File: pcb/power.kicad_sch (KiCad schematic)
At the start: 13 parts, among them J4 Conn_01x02, J5 ARM, U10 TPS2116DRL, U9 LM3671MF

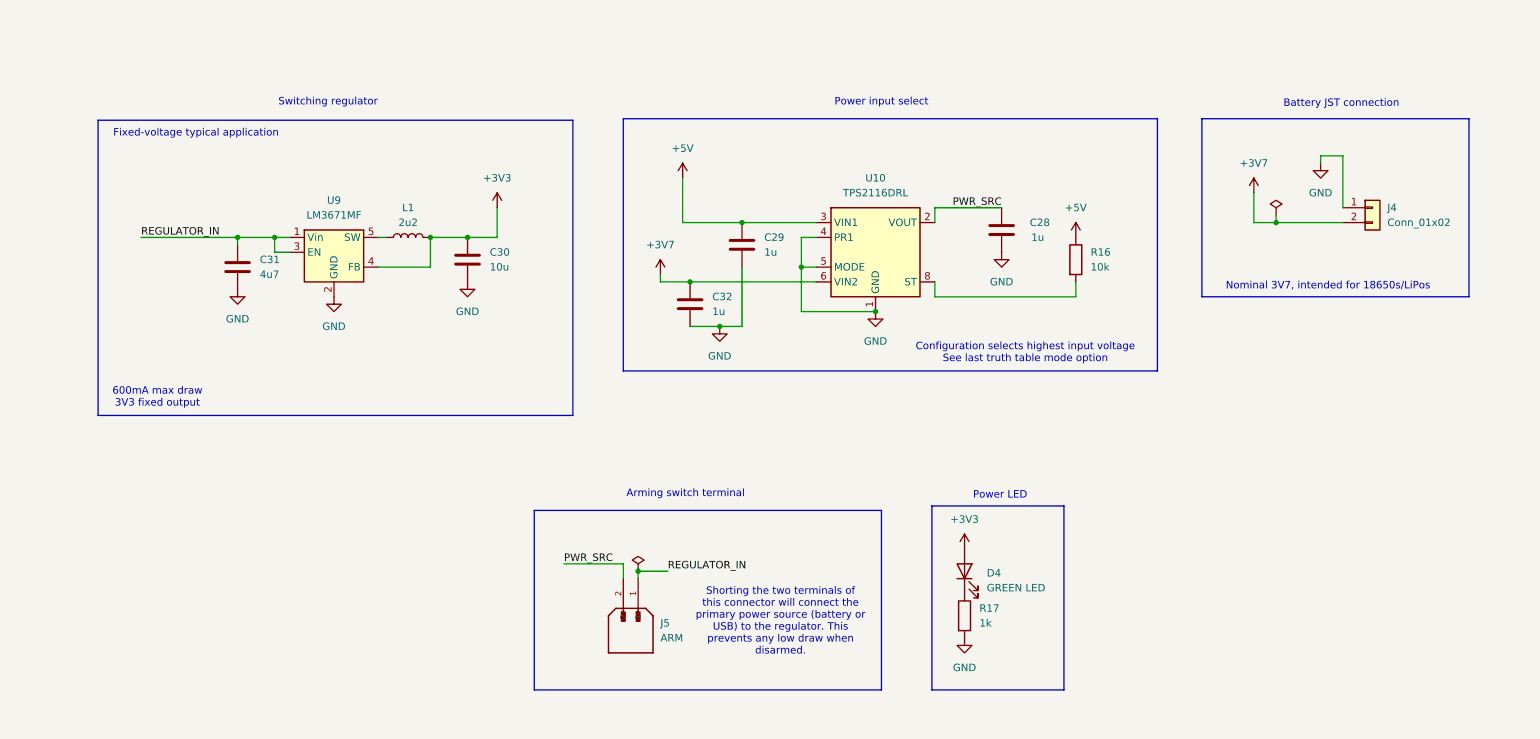
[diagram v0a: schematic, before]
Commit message: Filled out the BOM for the schematic. Consolidated some components and changed footprint sizes.
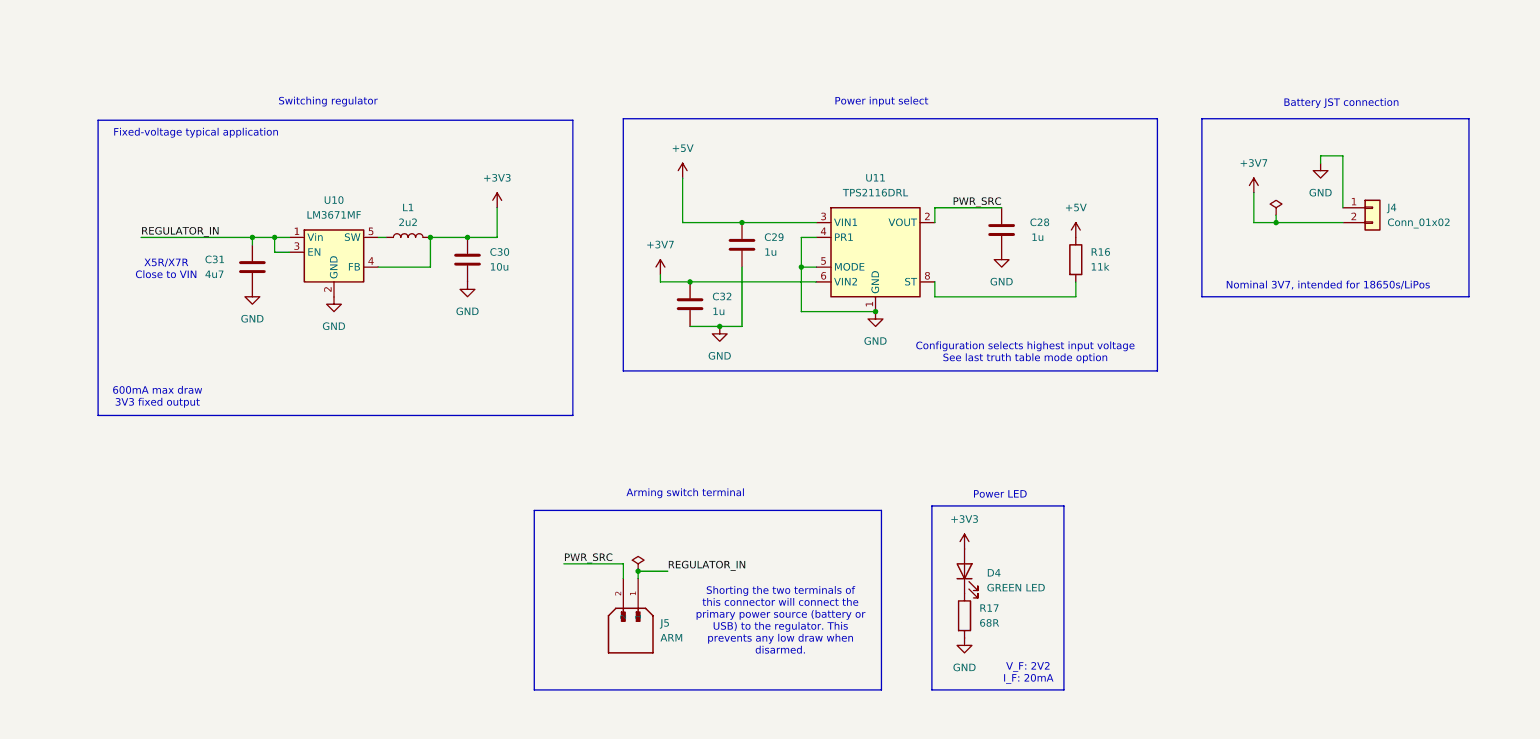
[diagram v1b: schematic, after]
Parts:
- C28, C29, C32: MP (none) -> 06036C105MAT2A
- C30: footprint Capacitor_SMD:C_0805_2012Metric -> Capacitor_SMD:C_0603_1608Metric; MP (none) -> C1608X5R0J106K080AB
- C31: MP (none) -> CGA3E1X5R0J475K080AC
- D4: MP (none) -> LG R971-KN-1
- J4: MP (none) -> S2B-PH-K-S(LF)(SN)(PP)
- J5: footprint TerminalBlock_Phoenix:TerminalBlock_Phoenix_MKDS-1,5-2_1x02_P5.00mm_Horizontal -> TerminalBlock_Phoenix:TerminalBlock_Phoenix_MKDS-3-2-5.08_1x02_P5.08mm_Horizontal; MP (none) -> 1711026
- L1: footprint Inductor_SMD:L_0805_2012Metric -> (none); MP (none) -> LPO3310-222MLC
- R16: value 10k -> 11k; footprint Resistor_SMD:R_0201_0603Metric -> Resistor_SMD:R_0402_1005Metric; MP (none) -> ERA-2AEB113X
- R17: value 1k -> 68R; footprint Resistor_SMD:R_0201_0603Metric -> Resistor_SMD:R_0402_1005Metric; MP (none) -> ERA-2AED680X
- U10: renamed from U9; MP (none) -> LM3671MF-3.3/NOPB
- U11: renamed from U10; MP (none) -> TPS2116DRLR
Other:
- note added: "V_F: 2V2 I_F: 20mA"
- note added: "X5R/X7R Close to VIN"
- moved on the sheet: C31

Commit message: Updated inductor footprint.
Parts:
- L1: footprint (none) -> LPO3310-222MLC:LPO3310222MLC
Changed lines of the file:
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@@
 			)
 		)
-		(property "Footprint" ""
+		(property "Footprint" "LPO3310-222MLC:LPO3310222MLC"
 			(at 85.09 73.66 0)
 			(effects

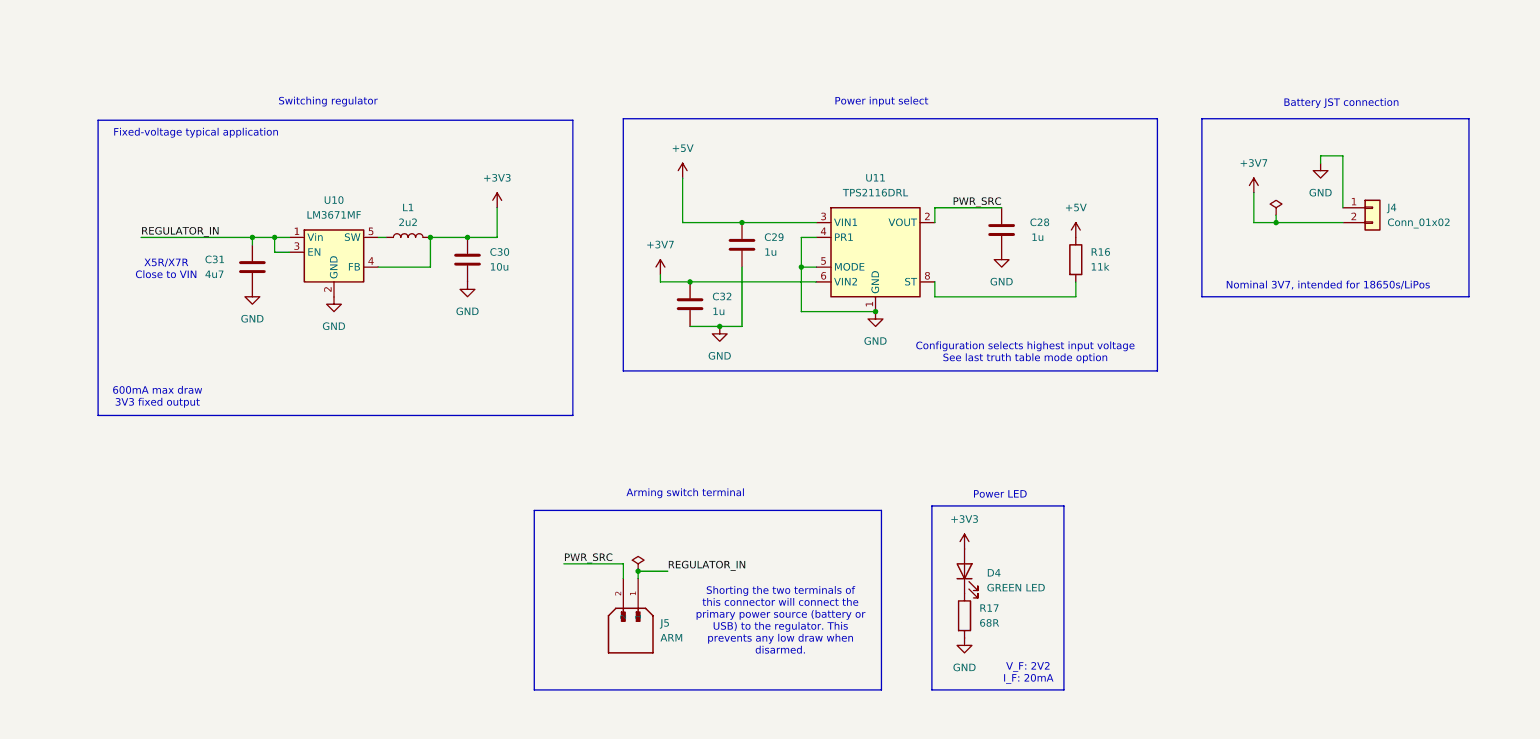
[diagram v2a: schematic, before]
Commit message: Added reverse polarity protection on JST connector
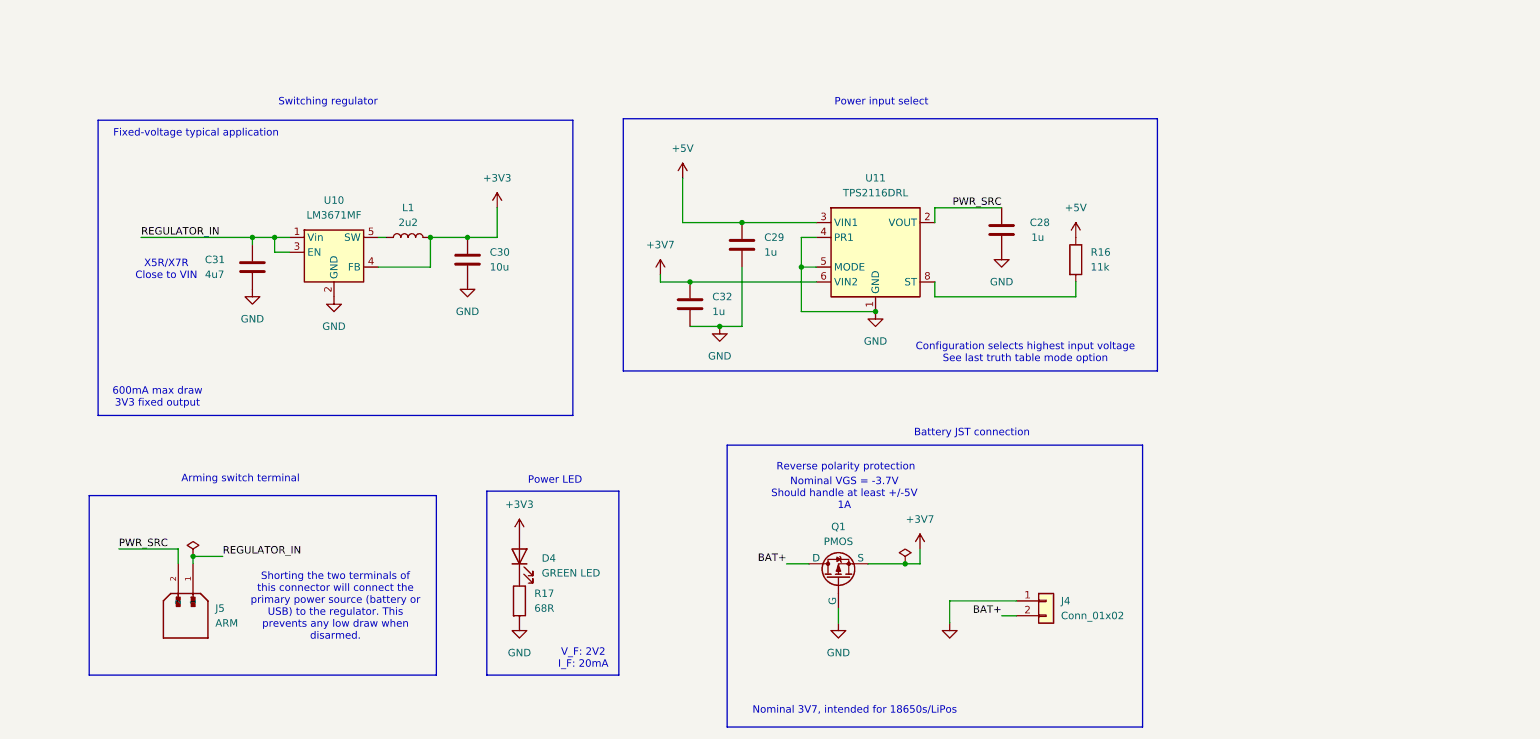
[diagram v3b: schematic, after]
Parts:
- added Q1: PMOS, Package_TO_SOT_SMD:SOT-23-3, symbol Simulation_SPICE:PMOS
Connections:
- net +3V7: now also Q1.3 (S); no longer J4.2 (Pin_2)
- net GND: now also Q1.2 (G)
- new net BAT+: J4.2 (Pin_2), Q1.1 (D)
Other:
- note added: "Nominal VGS = -3.7V Should handle at least +/-5V 1A"
- note added: "Reverse polarity protection"
- moved on the sheet: D4, J4, J5, R17

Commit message: Almost done routing
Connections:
- net +3V7: now also Q1.2 (S); no longer Q1.3 (S)
- net BAT+: now also Q1.3 (D); no longer Q1.1 (D)
- net GND: now also Q1.1 (G); no longer Q1.2 (G)
- net NSY_OUT: now reaches L1.1, U10.5 (SW)
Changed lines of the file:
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@@
+	)
+	(junction
+		(at 81.28 73.66)
+		(diameter 0)
+		(color 0 0 0 0)
 	)
 	(junction
@@
 	)
 	(junction
-		(at 88.9 73.66)
-		(diameter 0)
-		(color 0 0 0 0)
-	)
-	(junction
 		(at 165.1 86.36)
 		(diameter 0)
@@
 	)
 	(junction
+		(at 90.17 73.66)
+		(diameter 0)
+		(color 0 0 0 0)
+	)
+	(junction
 		(at 170.18 129.54)
 		(diameter 0)
@@
 	(wire
 		(pts
+			(xy 81.28 64.77) (xy 81.28 73.66)
+		)
+		(stroke
+			(width 0)
+			(type default)
+		)
+	)
+	(wire
+		(pts
 			(xy 199.39 83.82) (xy 199.39 81.28)
 		)
@@
 	(wire
 		(pts
-			(xy 88.9 73.66) (xy 88.9 78.74)
+			(xy 90.17 73.66) (xy 90.17 78.74)
 		)
 		(stroke
@@
 	(wire
 		(pts
+			(xy 90.17 73.66) (xy 95.25 73.66)
+		)
+		(stroke
+			(width 0)
+			(type default)
+		)
+	)
+	(wire
+		(pts
 			(xy 95.25 73.66) (xy 100.33 73.66)
 		)
@@
 	(wire
 		(pts
-			(xy 88.9 73.66) (xy 95.25 73.66)
-		)
-		(stroke
-			(width 0)
-			(type default)
-		)
-	)
-	(wire
-		(pts
 			(xy 142.24 78.74) (xy 142.24 88.9)
 		)
@@
 	(wire
 		(pts
-			(xy 80.01 78.74) (xy 88.9 78.74)
+			(xy 80.01 78.74) (xy 90.17 78.74)
+		)
+		(stroke
+			(width 0)
+			(type default)
+		)
+	)
+	(wire
+		(pts
+			(xy 90.17 73.66) (xy 88.9 73.66)
 		)
 		(stroke
@@
 	(label "REGULATOR_IN"
 		(at 53.34 128.27 0)
+		(fields_autoplaced yes)
+		(effects
+			(font
+				(size 1.27 1.27)
+			)
+			(justify left bottom)
+		)
+	)
+	(label "NSY_OUT"
+		(at 81.28 64.77 0)
 		(fields_autoplaced yes)
 		(effects
@@
 			)
 		)
-		(property "Sim.Pins" "1=D 2=G 3=S"
+		(property "Sim.Pins" "1=G 2=S 3=D"
 			(at 173.99 132.08 0)
 			(effects

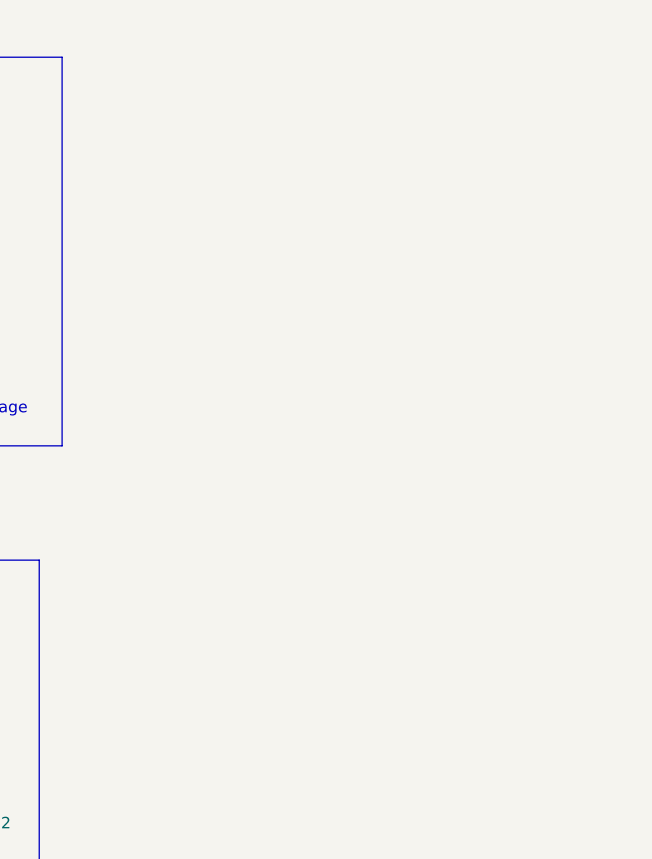
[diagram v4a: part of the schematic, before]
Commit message: Added test points and finished routing
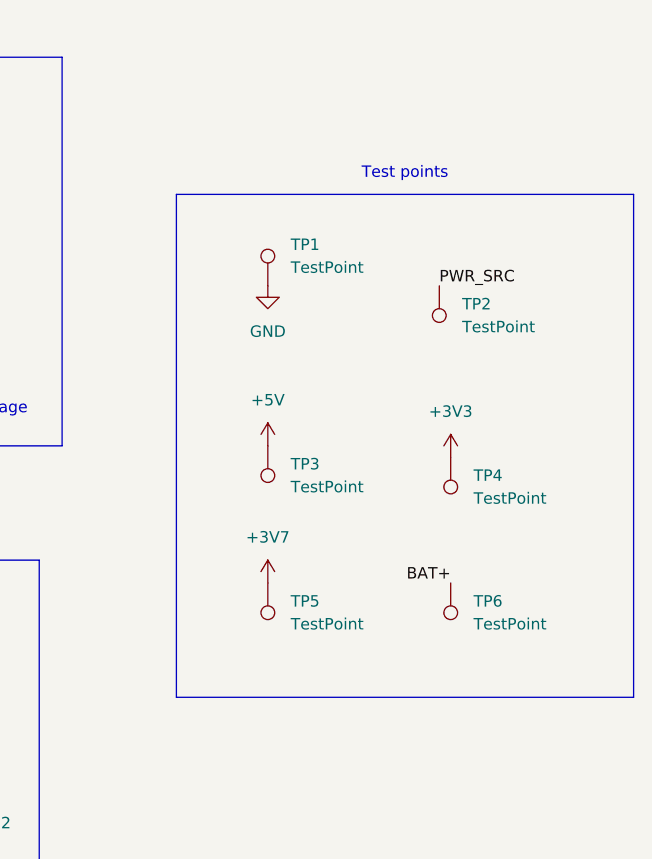
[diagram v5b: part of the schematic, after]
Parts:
- added TP1, TP2, TP4, TP5, TP6: TestPoint, TestPoint:TestPoint_Pad_D1.5mm, symbol Connector:TestPoint
- added TP3: TestPoint, TestPoint:TestPoint_Pad_D1.0mm, symbol Connector:TestPoint
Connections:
- net +3V3: now also TP4.1
- net +3V7: now also TP5.1
- net +5V: now also TP3.1
- net BAT+: now also TP6.1
- net GND: now also TP1.1
- net PWR_SRC: now also TP2.1
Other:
- note added: "Test points"

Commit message: Added battery charge monitor
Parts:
- added R21: 10k, Resistor_SMD:R_0402_1005Metric, symbol Device:R
- added R22: 33k, Resistor_SMD:R_0402_1005Metric, symbol Device:R
- added R23: 330R, Resistor_SMD:R_0402_1005Metric, symbol Device:R
- R16: value 11k -> 10k; MP ERA-2AEB113X -> SFR01MZPJ103
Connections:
- net BAT+: now also R21.2
- net GND: now also R23.2
- new net: R22.2, R23.1
- new net ADC0: R21.1, R22.1
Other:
- note added: "Battery monitor"
- note added: "Vout = 3V3 Vin = 4V2 (max)"
- moved on the sheet: C28, C29, C30, C31, C32, D4, J4, J5, L1, Q1, R16, R17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

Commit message: Battery charge detection after reverse polarity protection for safety.
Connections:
- net +3V7: now also R21.2
- net BAT+: no longer R21.2
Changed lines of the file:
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@@
 		)
 	)
-	(label "BAT+"
-		(at 226.06 115.57 180)
-		(fields_autoplaced yes)
-		(effects
-			(font
-				(size 1.27 1.27)
-			)
-			(justify right bottom)
-		)
-	)
 	(label "REGULATOR_IN"
 		(at 41.91 114.3 0)
@@
 					(unit 1)
 				)
+			)
+		)
+	)
+	(symbol
+		(lib_id "power:+3V3")
+		(at 226.06 115.57 0)
+		(unit 1)
+		(exclude_from_sim no)
+		(in_bom yes)
+		(on_board yes)
+		(dnp no)
+		(fields_autoplaced yes)
+		(property "Reference" "#PWR082"
+			(at 226.06 119.38 0)
+			(effects
+				(font
+					(size 1.27 1.27)
+				)
+				(hide yes)
+			)
+		)
+		(property "Value" "+3V7"
+			(at 226.06 110.49 0)
+			(effects
+				(font
+					(size 1.27 1.27)
+				)
+			)
+		)
+		(property "Footprint" ""
+			(at 226.06 115.57 0)
+			(effects
+				(font
+					(size 1.27 1.27)
+				)
+				(hide yes)
+			)
+		)
+		(property "Datasheet" ""
+			(at 226.06 115.57 0)
+			(effects
+				(font
+					(size 1.27 1.27)
+				)
+				(hide yes)
+			)
+		)
+		(property "Description" "Power symbol creates a global label with name \"+3V3\""
+			(at 226.06 115.57 0)
+			(effects
+				(font
+					(size 1.27 1.27)
+				)
+				(hide yes)
+			)
+		)
+		(pin "1"
+		)
+		(instances
+			(project "flight-computer"
+				(path "/b90d3133-97a4-4747-8a68-e80f353c7b97/8d42d8f3-e666-4352-a3e9-99ac4271efe0"
+					(reference "#PWR082")
+					(unit 1)
+				)

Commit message: Changed LED resistors to 330 ohms to reduce brightness.
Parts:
- R17: value 68R -> 330R; MP ERA-2AED680X -> 560112110231
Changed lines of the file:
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@@
 			)
 		)
-		(property "Value" "68R"
+		(property "Value" "330R"
 			(at 95.25 123.1899 0)
 			(effects
@@
 			)
 		)
-		(property "Datasheet" "https://www.mouser.ca/datasheet/2/315/AOA0000C307-1149632.pdf"
+		(property "Datasheet" "https://www.we-online.com/components/products/datasheet/560112110231.pdf"
 			(at 92.71 121.92 0)
 			(effects
@@
 			)
 		)
-		(property "MP" "ERA-2AED680X"
+		(property "MP" "560112110231"
 			(at 92.71 121.92 0)
 			(effects
